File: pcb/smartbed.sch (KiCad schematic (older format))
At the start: 53 parts, among them J1 USB_MICRO_A, J2 SBBUS_1, J3 DBGCON, J4 GPIOCON, J5 GPIOCON, J6 FSRCON1, J7 FSRCON2, J8 SBBUS_2, SW1 SW_SPST, U1 LD1117S33CTR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

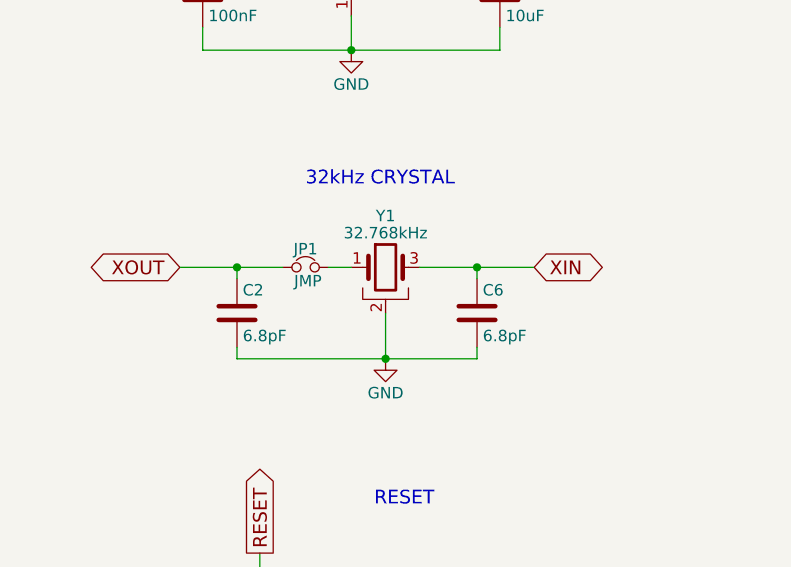
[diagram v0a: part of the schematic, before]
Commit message: Connected most of the traces
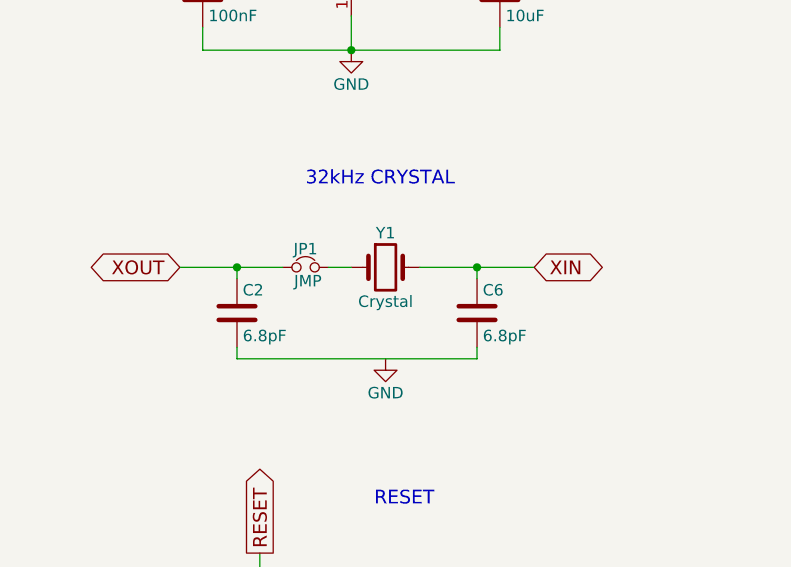
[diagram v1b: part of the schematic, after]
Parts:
- removed Y1: 32.768kHz, Crystals:Crystal_Round_d3.0mm_Vertical, symbol Crystal_GND2
- added Y1: Crystal, Crystals:Crystal_Round_d3.0mm_Vertical, symbol Crystal
- C1, C10, C11, C12, C2, C3, C4, C5, C6, C7, C8, C9: footprint Capacitors_SMD:C_0805_HandSoldering -> Capacitors_SMD:C_0603_HandSoldering
- J2, J8: footprint Pin_Headers:Pin_Header_Straight_2x03_Pitch2.54mm -> Connectors:IDC_Header_Straight_6pins
- J3: footprint Pin_Headers:Pin_Header_Straight_2x05_Pitch2.54mm -> Connectors:IDC_Header_Straight_10pins
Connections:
- net GND: no longer C2.2, C6.2
- net XIN: now also Y1.2
- net at JP1.2: now also Y1.1
- new net: C2.2, C6.2
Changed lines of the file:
@@
 F 0 "C8" H 2575 3450 50  0000 L CNN
 F 1 "10uF" H 2575 3250 50  0000 L CNN
-F 2 "Capacitors_SMD:C_0805_HandSoldering" H 2588 3200 50  0001 C CNN
+F 2 "Capacitors_SMD:C_0603_HandSoldering" H 2588 3200 50  0001 C CNN
 F 3 "" H 2550 3350 50  0001 C CNN
 	1    2550 3350
@@
 F 0 "C1" H 1275 3450 50  0000 L CNN
 F 1 "100nF" H 1275 3250 50  0000 L CNN
-F 2 "Capacitors_SMD:C_0805_HandSoldering" H 1288 3200 50  0001 C CNN
+F 2 "Capacitors_SMD:C_0603_HandSoldering" H 1288 3200 50  0001 C CNN
 F 3 "" H 1250 3350 50  0001 C CNN
 	1    1250 3350
@@
 F 0 "J2" H 1550 8150 50  0000 C CNN
 F 1 "SBBUS_1" H 1550 7750 50  0000 C CNN
-F 2 "Pin_Headers:Pin_Header_Straight_2x03_Pitch2.54mm" H 1550 6750 50  0001 C CNN
+F 2 "Connectors:IDC_Header_Straight_6pins" H 1550 6750 50  0001 C CNN
 F 3 "" H 1550 6750 50  0001 C CNN
 	1    1550 7950
@@
 F 0 "C2" H 1425 4850 50  0000 L CNN
 F 1 "6.8pF" H 1425 4650 50  0000 L CNN
-F 2 "Capacitors_SMD:C_0805_HandSoldering" H 1438 4600 50  0001 C CNN
+F 2 "Capacitors_SMD:C_0603_HandSoldering" H 1438 4600 50  0001 C CNN
 F 3 "" H 1400 4750 50  0001 C CNN
 	1    1400 4750
@@
 F 0 "C6" H 2475 4850 50  0000 L CNN
 F 1 "6.8pF" H 2475 4650 50  0000 L CNN
-F 2 "Capacitors_SMD:C_0805_HandSoldering" H 2488 4600 50  0001 C CNN
+F 2 "Capacitors_SMD:C_0603_HandSoldering" H 2488 4600 50  0001 C CNN
 F 3 "" H 2450 4750 50  0001 C CNN
 	1    2450 4750
@@
 	1    0    0    -1
 $EndComp
-$Comp
-L Crystal_GND2 Y1
-U 1 1 593AA73E
-P 2050 4550
-F 0 "Y1" H 2050 4775 50  0000 C CNN
-F 1 "32.768kHz" H 2050 4700 50  0000 C CNN
-F 2 "Crystals:Crystal_Round_d3.0mm_Vertical" H 2050 4550 50  0001 C CNN
-F 3 "" H 2050 4550 50  0001 C CNN
-	1    2050 4550
-	1    0    0    -1
-$EndComp
 Text Notes 1700 4200 0    60   ~ 0
 32kHz CRYSTAL
@@
 F 0 "C4" V 2350 6800 50  0000 L CNN
 F 1 "100nF" V 2050 6700 50  0000 L CNN
-F 2 "Capacitors_SMD:C_0805_HandSoldering" H 2238 6650 50  0001 C CNN
+F 2 "Capacitors_SMD:C_0603_HandSoldering" H 2238 6650 50  0001 C CNN
 F 3 "" H 2200 6800 50  0001 C CNN
 	1    2200 6800
@@
 F 0 "C12" H 9100 2000 50  0000 L CNN
 F 1 "100nF" H 9050 2200 50  0000 L CNN
-F 2 "Capacitors_SMD:C_0805_HandSoldering" H 9088 1950 50  0001 C CNN
+F 2 "Capacitors_SMD:C_0603_HandSoldering" H 9088 1950 50  0001 C CNN
 F 3 "" H 9050 2100 50  0001 C CNN
 	1    9050 2100
@@
 F 0 "J3" H 3000 8300 50  0000 C CNN
 F 1 "DBGCON" H 3000 7700 50  0000 C CNN
-F 2 "Pin_Headers:Pin_Header_Straight_2x05_Pitch2.54mm" H 3000 6800 50  0001 C CNN
+F 2 "Connectors:IDC_Header_Straight_10pins" H 3000 6800 50  0001 C CNN
 F 3 "" H 3000 6800 50  0001 C CNN
 	1    3000 8000
@@
 F 0 "C11" H 6725 5350 50  0000 L CNN
 F 1 "100nF" H 6725 5150 50  0000 L CNN
-F 2 "Capacitors_SMD:C_0805_HandSoldering" H 6738 5100 50  0001 C CNN
+F 2 "Capacitors_SMD:C_0603_HandSoldering" H 6738 5100 50  0001 C CNN
 F 3 "" H 6700 5250 50  0001 C CNN
 	1    6700 5250
@@
 F 0 "C7" H 2525 9950 50  0000 L CNN
 F 1 "100nF" H 2525 9750 50  0000 L CNN
-F 2 "Capacitors_SMD:C_0805_HandSoldering" H 2538 9700 50  0001 C CNN
+F 2 "Capacitors_SMD:C_0603_HandSoldering" H 2538 9700 50  0001 C CNN
 F 3 "" H 2500 9850 50  0001 C CNN
 	1    2500 9850
@@
 F 0 "C5" H 2225 9950 50  0000 L CNN
 F 1 "100nF" H 2225 9750 50  0000 L CNN
-F 2 "Capacitors_SMD:C_0805_HandSoldering" H 2238 9700 50  0001 C CNN
+F 2 "Capacitors_SMD:C_0603_HandSoldering" H 2238 9700 50  0001 C CNN
 F 3 "" H 2200 9850 50  0001 C CNN
 	1    2200 9850
@@
 F 0 "C10" H 3125 9950 50  0000 L CNN
 F 1 "100nF" H 3125 9750 50  0000 L CNN
-F 2 "Capacitors_SMD:C_0805_HandSoldering" H 3138 9700 50  0001 C CNN
+F 2 "Capacitors_SMD:C_0603_HandSoldering" H 3138 9700 50  0001 C CNN
 F 3 "" H 3100 9850 50  0001 C CNN
 	1    3100 9850
@@
 F 0 "C9" H 2825 9950 50  0000 L CNN
 F 1 "100nF" H 2825 9750 50  0000 L CNN
-F 2 "Capacitors_SMD:C_0805_HandSoldering" H 2838 9700 50  0001 C CNN
+F 2 "Capacitors_SMD:C_0603_HandSoldering" H 2838 9700 50  0001 C CNN
 F 3 "" H 2800 9850 50  0001 C CNN
 	1    2800 9850
@@
 F 0 "C3" H 1525 1100 50  0000 L CNN
 F 1 "100nF" H 1525 900 50  0000 L CNN
-F 2 "Capacitors_SMD:C_0805_HandSoldering" H 1538 850 50  0001 C CNN
+F 2 "Capacitors_SMD:C_0603_HandSoldering" H 1538 850 50  0001 C CNN
 F 3 "" H 1500 1000 50  0001 C CNN
 	1    1500 1000
@@
 	2850 2150 2850 1200
 Wire Wire Line
-	2050 4750 2050 4950
-Wire Wire Line
 	2450 4550 2450 4600
 Wire Wire Line
 	2450 4950 2450 4900
-Connection ~ 2050 4950
 Wire Wire Line
 	1400 4950 2450 4950
@@
 F 0 "J8" H 1550 8750 50  0000 C CNN
 F 1 "SBBUS_2" H 1550 8350 50  0000 C CNN
-F 2 "Pin_Headers:Pin_Header_Straight_2x03_Pitch2.54mm" H 1550 7350 50  0001 C CNN
+F 2 "Connectors:IDC_Header_Straight_6pins" H 1550 7350 50  0001 C CNN
 F 3 "" H 1550 7350 50  0001 C CNN
 	1    1550 8550
@@
 	1450 1800 1450 1400
 Connection ~ 1450 1400
+$Comp
+L Crystal Y1
+U 1 1 59457367
+P 2050 4550
+F 0 "Y1" H 2050 4700 50  0000 C CNN
+F 1 "Crystal" H 2050 4400 50  0000 C CNN
+F 2 "Crystals:Crystal_Round_d3.0mm_Vertical" H 2050 4550 50  0001 C CNN
+F 3 "" H 2050 4550 50  0001 C CNN
+	1    2050 4550
+	1    0    0    -1
+$EndComp
 $EndSCHEMATC

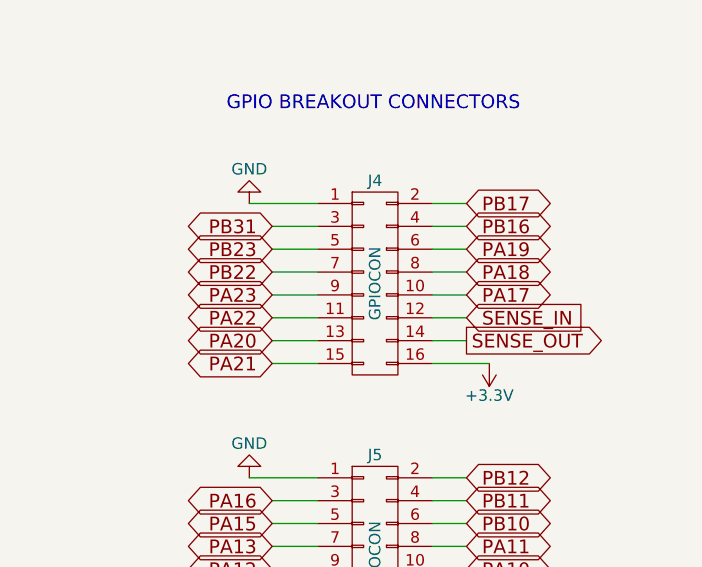
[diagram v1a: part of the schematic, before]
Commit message: Routed the board
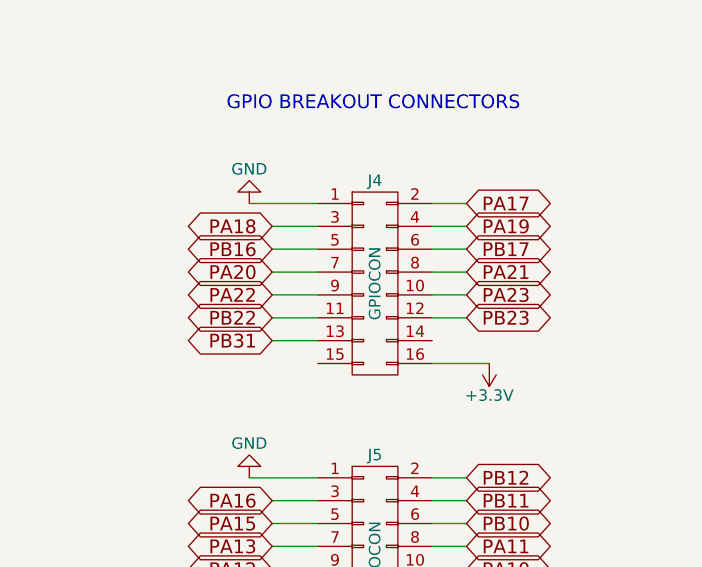
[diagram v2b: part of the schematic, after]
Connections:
- net PA17: now also J4.2 (P2); no longer J4.10 (P10)
- net PA18: now also J4.3 (P3); no longer J4.8 (P8)
- net PA19: now also J4.4 (P4); no longer J4.6 (P6)
- net PA20: now also J4.7 (P7); no longer J4.13 (P13)
- net PA21: now also J4.8 (P8); no longer J4.15 (P15)
- net PA22: now also J4.9 (P9); no longer J4.11 (P11)
- net PA23: now also J4.10 (P10); no longer J4.9 (P9)
- net PB16: now also J4.5 (P5); no longer J4.4 (P4)
- net PB17: now also J4.6 (P6); no longer J4.2 (P2)
- net PB22: now also J4.11 (P11); no longer J4.7 (P7)
- net PB23: now also J4.12 (P12); no longer J4.5 (P5)
- net PB31: now also J4.13 (P13); no longer J4.3 (P3)
- net SENSE_IN: no longer J4.12 (P12)
- net SENSE_OUT: no longer J4.14 (P14)
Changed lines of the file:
@@
 Text GLabel 8350 6550 3    60   BiDi ~ 0
 PA10
+Text GLabel 13850 8000 0    60   BiDi ~ 0
+PB31
+Text GLabel 14700 7900 2    60   BiDi ~ 0
+PB23
+Text GLabel 13850 7900 0    60   BiDi ~ 0
+PB22
+Text GLabel 13850 7800 0    60   BiDi ~ 0
+PA22
+Text GLabel 14700 7800 2    60   BiDi ~ 0
+PA23
+Text GLabel 14700 7700 2    60   BiDi ~ 0
+PA21
+Text GLabel 13850 7700 0    60   BiDi ~ 0
+PA20
+Text GLabel 14700 7600 2    60   BiDi ~ 0
+PB17
+Text GLabel 13850 7600 0    60   BiDi ~ 0
+PB16
+Text GLabel 14700 7500 2    60   BiDi ~ 0
+PA19
 Text GLabel 13850 7500 0    60   BiDi ~ 0
-PB31
-Text GLabel 13850 7600 0    60   BiDi ~ 0
-PB23
-Text GLabel 13850 7700 0    60   BiDi ~ 0
-PB22
-Text GLabel 13850 7900 0    60   BiDi ~ 0
-PA22
-Text GLabel 13850 7800 0    60   BiDi ~ 0
-PA23
-Text GLabel 13850 8100 0    60   BiDi ~ 0
-PA21
-Text GLabel 13850 8000 0    60   BiDi ~ 0
-PA20
+PA18
 Text GLabel 14700 7400 2    60   BiDi ~ 0
-PB17
-Text GLabel 14700 7500 2    60   BiDi ~ 0
-PB16
-Text GLabel 14700 7600 2    60   BiDi ~ 0
-PA19
-Text GLabel 14700 7700 2    60   BiDi ~ 0
-PA18
-Text GLabel 14700 7800 2    60   BiDi ~ 0
 PA17
 $Comp
@@
 	14800 9300 14550 9300
 Wire Wire Line
-	14050 8100 13850 8100
-Wire Wire Line
 	13850 8000 14050 8000
 Wire Wire Line
@@
 Wire Wire Line
 	14550 7900 14700 7900
-Wire Wire Line
-	14700 8000 14550 8000
 Wire Wire Line
 	8350 6350 8350 6550
@@
 Wire Wire Line
 	14050 7900 13850 7900
-Text GLabel 14700 7900 2    60   Input ~ 0
-SENSE_IN
-Text GLabel 14700 8000 2    60   Output ~ 0
-SENSE_OUT
 Text GLabel 9550 6900 3    60   Input ~ 0
 VBUS

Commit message: Revision 2
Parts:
- removed J4, J5: GPIOCON, Pin_Headers:Pin_Header_Straight_2x08_Pitch2.54mm, symbol CONN_02X08
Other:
- note removed: "GPIO BREAKOUT CONNECTORS"
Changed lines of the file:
@@
 Text GLabel 9450 3400 1    60   Output ~ 0
 SENSE_OUT
-$Comp
-L CONN_02X08 J4
-U 1 1 5941D25D
-P 14300 7750
-F 0 "J4" H 14300 8200 50  0000 C CNN
-F 1 "GPIOCON" V 14300 7750 50  0000 C CNN
-F 2 "Pin_Headers:Pin_Header_Straight_2x08_Pitch2.54mm" H 14300 6550 50  0001 C CNN
-F 3 "" H 14300 6550 50  0001 C CNN
-	1    14300 7750
-	1    0    0    -1
-$EndComp
-$Comp
-L GND #PWR043
-U 1 1 5941F26B
-P 13750 7400
-F 0 "#PWR043" H 13750 7150 50  0001 C CNN
-F 1 "GND" H 13750 7250 50  0000 C CNN
-F 2 "" H 13750 7400 50  0001 C CNN
-F 3 "" H 13750 7400 50  0001 C CNN
-	1    13750 7400
-	-1   0    0    1
-$EndComp
-$Comp
-L +3.3V #PWR044
-U 1 1 5941F3AB
-P 14800 8100
-F 0 "#PWR044" H 14800 7950 50  0001 C CNN
-F 1 "+3.3V" H 14800 8240 50  0000 C CNN
-F 2 "" H 14800 8100 50  0001 C CNN
-F 3 "" H 14800 8100 50  0001 C CNN
-	1    14800 8100
-	-1   0    0    1
-$EndComp
 Text GLabel 8550 3800 1    60   BiDi ~ 0
 PB31
@@
 Text GLabel 8350 6550 3    60   BiDi ~ 0
 PA10
-Text GLabel 13850 8000 0    60   BiDi ~ 0
-PB31
-Text GLabel 14700 7900 2    60   BiDi ~ 0
-PB23
-Text GLabel 13850 7900 0    60   BiDi ~ 0
-PB22
-Text GLabel 13850 7800 0    60   BiDi ~ 0
-PA22
-Text GLabel 14700 7800 2    60   BiDi ~ 0
-PA23
-Text GLabel 14700 7700 2    60   BiDi ~ 0
-PA21
-Text GLabel 13850 7700 0    60   BiDi ~ 0
-PA20
-Text GLabel 14700 7600 2    60   BiDi ~ 0
-PB17
-Text GLabel 13850 7600 0    60   BiDi ~ 0
-PB16
-Text GLabel 14700 7500 2    60   BiDi ~ 0
-PA19
-Text GLabel 13850 7500 0    60   BiDi ~ 0
-PA18
-Text GLabel 14700 7400 2    60   BiDi ~ 0
-PA17
-$Comp
-L CONN_02X08 J5
-U 1 1 594275D8
-P 14300 8950
-F 0 "J5" H 14300 9400 50  0000 C CNN
-F 1 "GPIOCON" V 14300 8950 50  0000 C CNN
-F 2 "Pin_Headers:Pin_Header_Straight_2x08_Pitch2.54mm" H 14300 7750 50  0001 C CNN
-F 3 "" H 14300 7750 50  0001 C CNN
-	1    14300 8950
-	1    0    0    -1
-$EndComp
-$Comp
-L GND #PWR045
-U 1 1 594275DE
-P 13750 8600
-F 0 "#PWR045" H 13750 8350 50  0001 C CNN
-F 1 "GND" H 13750 8450 50  0000 C CNN
-F 2 "" H 13750 8600 50  0001 C CNN
-F 3 "" H 13750 8600 50  0001 C CNN
-	1    13750 8600
-	-1   0    0    1
-$EndComp
-$Comp
-L +3.3V #PWR046
-U 1 1 594275E4
-P 14800 9300
-F 0 "#PWR046" H 14800 9150 50  0001 C CNN
-F 1 "+3.3V" H 14800 9440 50  0000 C CNN
-F 2 "" H 14800 9300 50  0001 C CNN
-F 3 "" H 14800 9300 50  0001 C CNN
-	1    14800 9300
-	-1   0    0    1
-$EndComp
-Text GLabel 13850 8700 0    60   BiDi ~ 0
-PA16
-Text GLabel 13850 8800 0    60   BiDi ~ 0
-PA15
-Text GLabel 13850 8900 0    60   BiDi ~ 0
-PA13
-Text GLabel 13850 9000 0    60   BiDi ~ 0
-PA12
-Text GLabel 13850 9100 0    60   BiDi ~ 0
-PB15
-Text GLabel 13850 9200 0    60   BiDi ~ 0
-PB14
-Text GLabel 13850 9300 0    60   BiDi ~ 0
-PB13
-Text GLabel 14700 8600 2    60   BiDi ~ 0
-PB12
-Text GLabel 14700 8700 2    60   BiDi ~ 0
-PB11
-Text GLabel 14700 8800 2    60   BiDi ~ 0
-PB10
-Text GLabel 14700 8900 2    60   BiDi ~ 0
-PA11
-Text GLabel 14700 9000 2    60   BiDi ~ 0
-PA10
-Text GLabel 14700 9100 2    60   Input ~ 0
-SCL
-Text GLabel 14700 9200 2    60   BiDi ~ 0
-SDA
-Text Notes 13650 7000 0    60   ~ 0
-GPIO BREAKOUT CONNECTORS
 Wire Wire Line
 	8550 6350 8550 7550
 Wire Wire Line
-	14050 9300 13850 9300
-Wire Wire Line
-	13850 9200 14050 9200
-Wire Wire Line
-	14050 9100 13850 9100
-Wire Wire Line
-	13850 9000 14050 9000
-Wire Wire Line
-	14050 8900 13850 8900
-Wire Wire Line
-	13850 8800 14050 8800
-Wire Wire Line
-	14050 8700 13850 8700
-Wire Wire Line
-	14700 8600 14550 8600
-Wire Wire Line
-	14550 8700 14700 8700
-Wire Wire Line
-	14700 8800 14550 8800
-Wire Wire Line
-	14550 8900 14700 8900
-Wire Wire Line
-	14700 9000 14550 9000
-Wire Wire Line
-	14550 9100 14700 9100
-Wire Wire Line
-	14700 9200 14550 9200
-Wire Wire Line
-	14050 8600 13750 8600
-Wire Wire Line
-	14800 9300 14550 9300
-Wire Wire Line
-	13850 8000 14050 8000
-Wire Wire Line
-	14050 7700 13850 7700
-Wire Wire Line
-	13850 7600 14050 7600
-Wire Wire Line
-	14050 7500 13850 7500
-Wire Wire Line
-	14700 7400 14550 7400
-Wire Wire Line
-	14550 7500 14700 7500
-Wire Wire Line
-	14700 7600 14550 7600
-Wire Wire Line
-	14550 7700 14700 7700
-Wire Wire Line
-	14700 7800 14550 7800
-Wire Wire Line
-	14550 7900 14700 7900
-Wire Wire Line
 	8350 6350 8350 6550
 Wire Wire Line
@@
 Wire Wire Line
 	8550 3800 8550 3900
-Wire Wire Line
-	14050 7400 13750 7400
-Wire Wire Line
-	14800 8100 14550 8100
 Wire Wire Line
 	9450 3900 9450 3400
@@
 Wire Wire Line
 	9150 3900 9150 2700
-Wire Wire Line
-	14050 7800 13850 7800
-Wire Wire Line
-	14050 7900 13850 7900
 Text GLabel 9550 6900 3    60   Input ~ 0
 VBUS

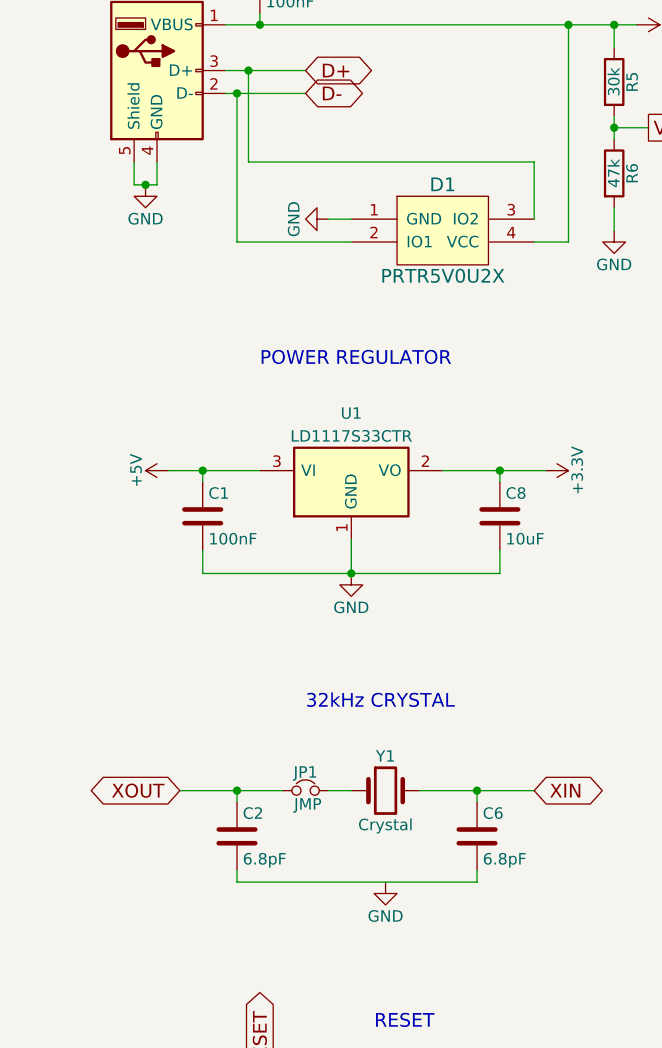
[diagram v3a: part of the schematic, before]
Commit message: Minor changes to PCB, added HTML BOM
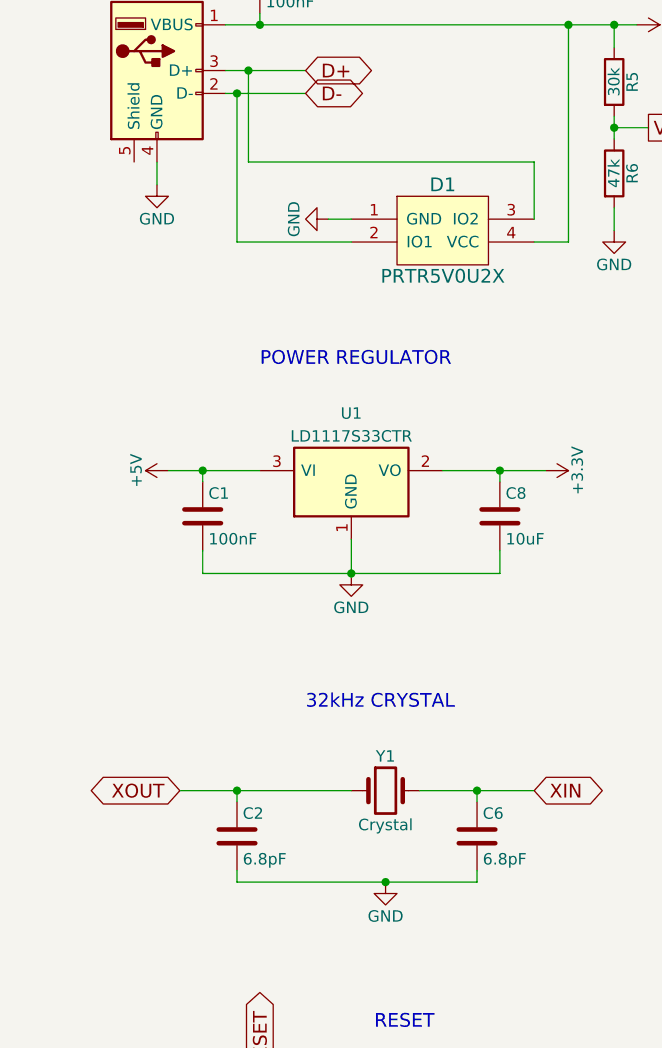
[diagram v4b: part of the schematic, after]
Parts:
- removed JP1: JMP, Pin_Headers:Pin_Header_Straight_1x02_Pitch2.54mm, symbol Jumper_NC_Small
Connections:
- net GND: now also C2.2, C6.2; no longer J1.5 (Shield)
- net XOUT: now also Y1.1
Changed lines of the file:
@@
 L GND #PWR02
 U 1 1 593A6E3B
-P 1000 1900
-F 0 "#PWR02" H 1000 1650 50  0001 C CNN
-F 1 "GND" H 1000 1750 50  0000 C CNN
-F 2 "" H 1000 1900 50  0001 C CNN
-F 3 "" H 1000 1900 50  0001 C CNN
-	1    1000 1900
+P 1050 1900
+F 0 "#PWR02" H 1050 1650 50  0001 C CNN
+F 1 "GND" H 1050 1750 50  0000 C CNN
+F 2 "" H 1050 1900 50  0001 C CNN
+F 3 "" H 1050 1900 50  0001 C CNN
+	1    1050 1900
 	1    0    0    -1
 $EndComp
@@
 Text Notes 2000 5600 0    60   ~ 0
 RESET
-$Comp
-L Jumper_NC_Small JP1
-U 1 1 593AECBC
-P 1700 4550
-F 0 "JP1" H 1700 4630 50  0000 C CNN
-F 1 "JMP" H 1710 4490 50  0000 C CNN
-F 2 "Pin_Headers:Pin_Header_Straight_1x02_Pitch2.54mm" H 1700 4550 50  0001 C CNN
-F 3 "" H 1700 4550 50  0001 C CNN
-	1    1700 4550
-	1    0    0    -1
-$EndComp
 Text GLabel 1150 4550 0    60   BiDi ~ 0
 XOUT
@@
 	1400 4550 1400 4600
 Wire Wire Line
-	1150 4550 1600 4550
-Wire Wire Line
-	1800 4550 1900 4550
+	1150 4550 1900 4550
 Connection ~ 2600 6350
 Wire Wire Line
@@
 Wire Wire Line
 	2700 2050 2700 1800
-Connection ~ 1000 1900
 Wire Wire Line
 	1050 1900 1050 1800
-Wire Wire Line
-	950  1900 1050 1900
-Wire Wire Line
-	950  1800 950  1900
 Wire Wire Line
 	1900 3450 1900 3600
@@
 	3050 1700 3050 1600
 $Comp
-L GND #PWR047
+L GND #PWR043
 U 1 1 5943F29D
 P 3050 2100
-F 0 "#PWR047" H 3050 1850 50  0001 C CNN
+F 0 "#PWR043" H 3050 1850 50  0001 C CNN
 F 1 "GND" H 3050 1950 50  0000 C CNN
 F 2 "" H 3050 2100 50  0001 C CNN
@@
 $EndComp
 $Comp
-L GND #PWR048
+L GND #PWR044
 U 1 1 59444009
 P 1900 8650
-F 0 "#PWR048" H 1900 8400 50  0001 C CNN
+F 0 "#PWR044" H 1900 8400 50  0001 C CNN
 F 1 "GND" H 1900 8500 50  0000 C CNN
 F 2 "" H 1900 8650 50  0001 C CNN
@@
 SENSE_OUT
 $Comp
-L +5V #PWR049
+L +5V #PWR045
 U 1 1 59444013
 P 1200 8450
-F 0 "#PWR049" H 1200 8300 50  0001 C CNN
+F 0 "#PWR045" H 1200 8300 50  0001 C CNN
 F 1 "+5V" H 1200 8590 50  0000 C CNN
 F 2 "" H 1200 8450 50  0001 C CNN
@@
 	1    0    0    -1
 $EndComp
+Connection ~ 2050 4950
 $EndSCHEMATC
